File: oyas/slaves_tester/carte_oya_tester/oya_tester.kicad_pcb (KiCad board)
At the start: 2 copper layers, 99 x 99 mm, 54 parts, among them J1 Power, J2 Bus Oya, J3 Power_Bus, J4 ON_OFF, SW3 Address, SW4 Select, U1 D148K, U2 MAX485E, U3 BPC_Alim5V, X1 Trou, X2 Trou, X3 Trou, X4 Trou

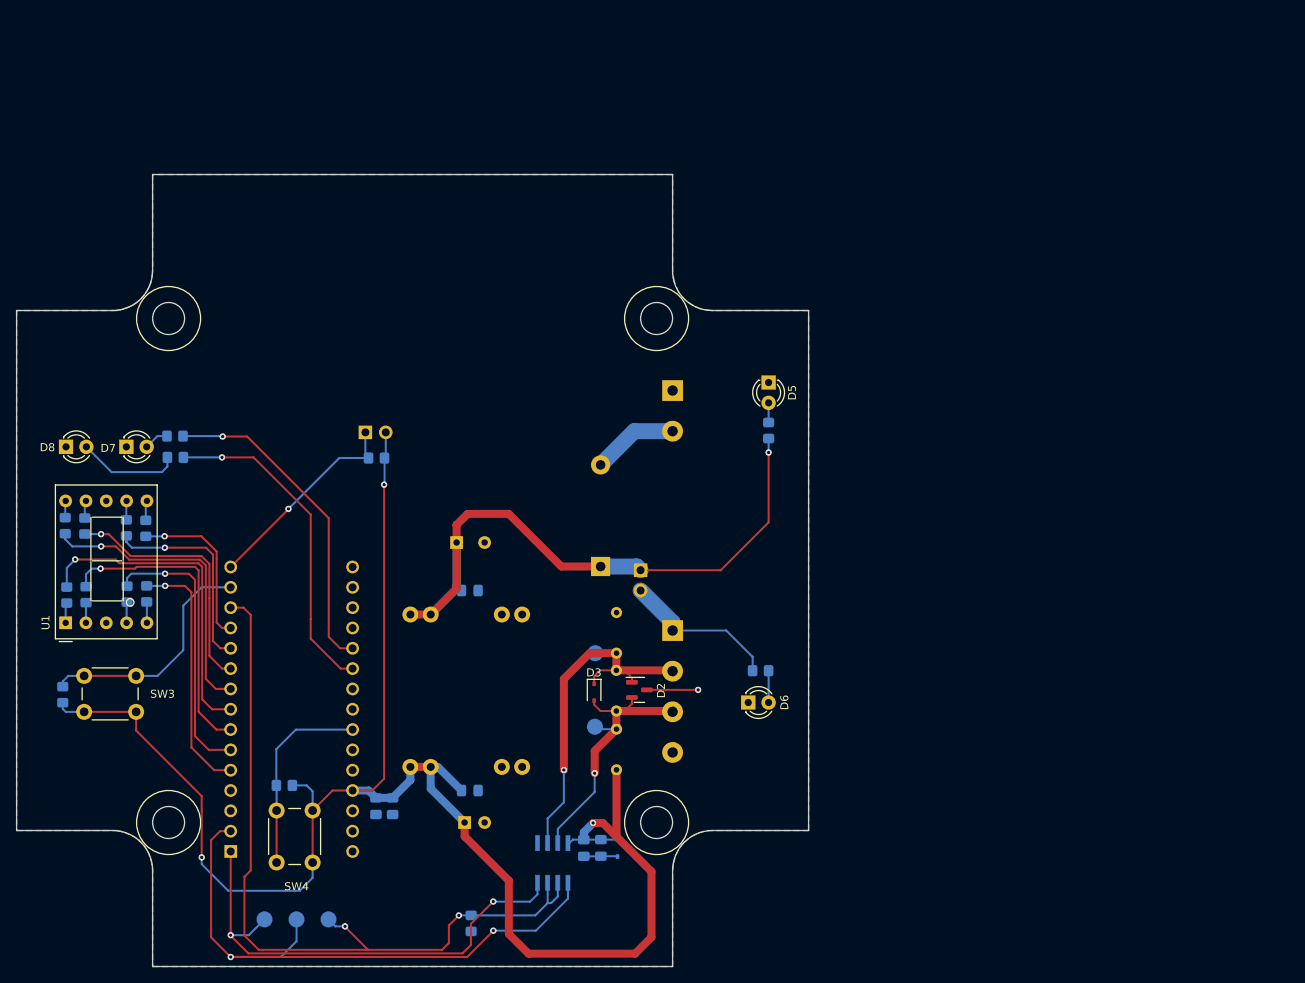
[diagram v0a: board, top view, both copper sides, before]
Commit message: Finalisation testeur Connecteurs des interrupteurs à choisir...
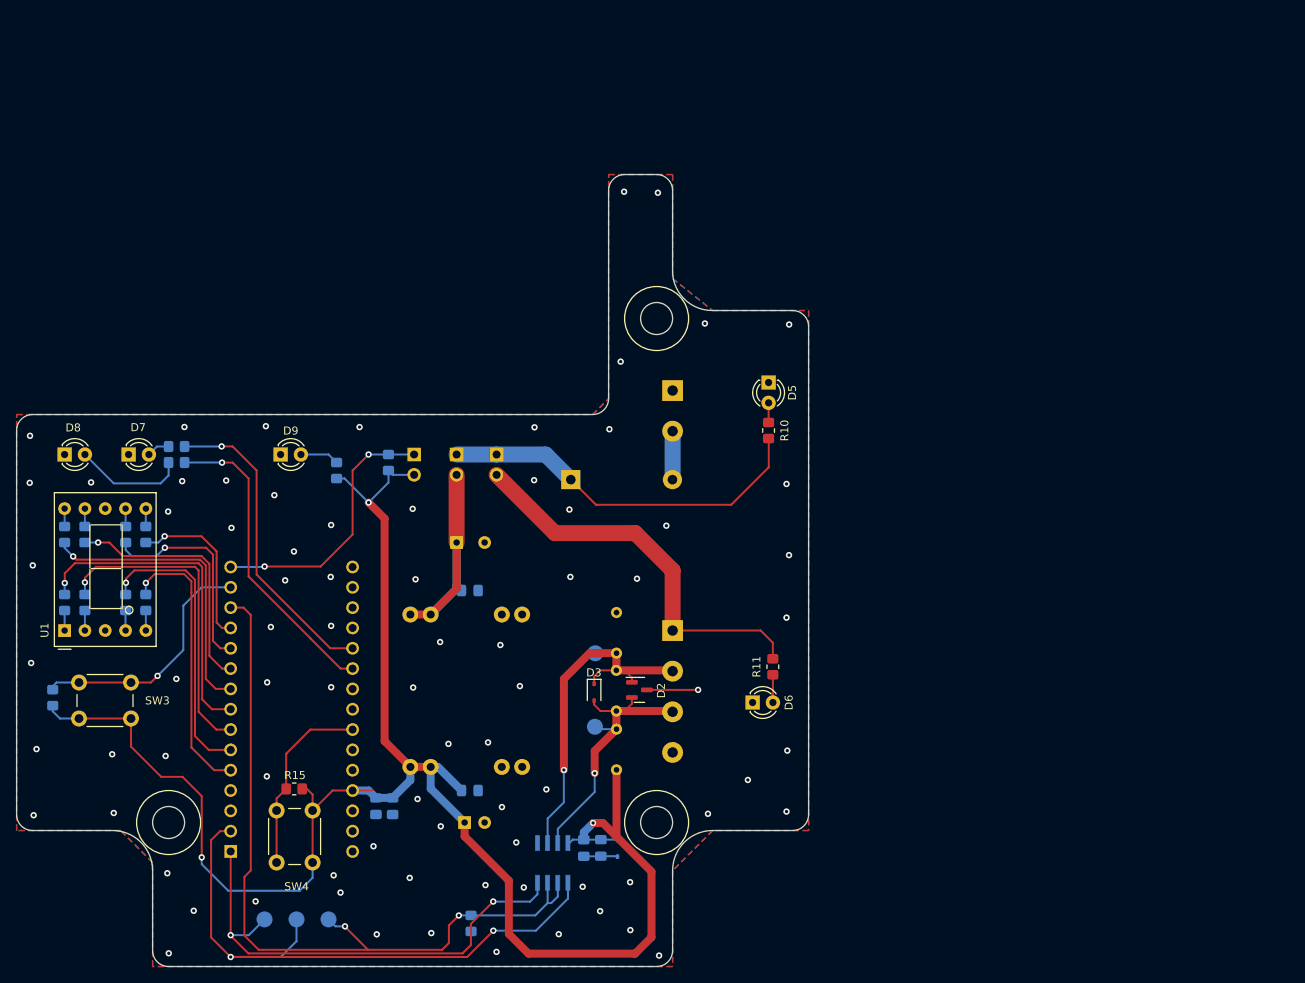
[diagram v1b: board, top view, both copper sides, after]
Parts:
- removed X1: Trou, bpc:BPC_Trou4mm_Fixation
- added D9: LED Rouge, LED_THT:LED_D3.0mm_FlatTop, F.Cu at (71.0, 98.0)
- added J5: Power_Cpu, Connector_PinHeader_2.54mm:PinHeader_1x02_P2.54mm_Vertical, B.Cu at (93.0, 98.0)
- added R20: 220, Resistor_SMD:R_0805_2012Metric_Pad1.20x1.40mm_HandSolder, B.Cu at (78.0, 100.0)
- R10, R11, R15: moved to F.Cu
- R12, R13: value 1k -> 220
- moved J3 23.1 mm to (98.0, 98.0)
- moved D4 11.5 mm to (107.3, 101.1), turned to 0 degrees
- moved J4 6.69 mm to (87.7, 98.0), turned to 180 degrees
- moved R11 1.61 mm to (132.5, 124.5), turned to -90 degrees
- moved R16 1.59 mm to (84.5, 99.0), turned to 90 degrees
- moved R12 1.32 mm to (58.0, 97.0)
- moved R14 1.31 mm to (42.5, 128.4)
- moved R15 1.31 mm to (72.7, 139.8)
- moved R7 1.10 mm to (44.0, 108.0)
- moved R8 1.09 mm to (54.1, 116.5)
- moved R3 1.07 mm to (51.6, 116.5)
- moved R6 1.06 mm to (46.5, 108.0)
- moved SW3 1.05 mm to (52.3, 131.0)
- moved D7 1.00 mm to (52.0, 98.0)
- moved R4 0.99 mm to (46.5, 116.5)
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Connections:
- C5 pad 1: POWER_12V -> Net-(J5-Pin_2)
- C8 pad 1: POWER_12V -> Net-(J5-Pin_2)
- U3 pad 1: POWER_12V -> Net-(J5-Pin_2)
- U3 pad 2: POWER_12V -> Net-(J5-Pin_2)
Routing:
- net POWER_12V: track 81.8 -> 47.2 mm, vias 1 -> 0
- net Net-(J5-Pin_2): track 0.00 -> 32.6 mm
- net Net-(J2-Pin_1): track 19.7 -> 49.6 mm
- net ON_OFF: track 26.3 -> 33.4 mm, vias 1 -> 2
- net Net-(D9-A): track 0.00 -> 4.87 mm
- net Net-(D4-A): track 10.7 -> 6.07 mm
- net +5V: track 213.8 -> 217.4 mm
- net SEG_DP: track 31.4 -> 34.8 mm
- net Net-(A1-A2): track 41.2 -> 38.8 mm
- net Net-(A1-A1): track 40.9 -> 39.1 mm
- net SEG_C: track 34.8 -> 36.3 mm
- net CHANGE_ADDRESS: track 29.8 -> 31.1 mm, vias 0 -> 1
- net Net-(D8-A): track 12.9 -> 14.0 mm
- net SELECT: track 24.7 -> 23.6 mm
- net SEG_D: track 38.8 -> 39.7 mm
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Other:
- outline, holes or cut-outs redrawn

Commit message: Finition
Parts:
- removed J3: Power_Bus, Connector_PinHeader_2.54mm:PinHeader_1x02_P2.54mm_Vertical
- removed J4: ON_OFF, Connector_PinHeader_2.54mm:PinHeader_1x02_P2.54mm_Vertical
- removed J5: Power_Cpu, Connector_PinHeader_2.54mm:PinHeader_1x02_P2.54mm_Vertical
- added C9: 1000µF, Capacitor_THT:CP_Radial_D16.0mm_P7.50mm, B.Cu at (116.6, 108.3)
- added J6: Switches, Connector_JST:JST_VH_B6P-VH-FB-B_1x06_P3.96mm_Vertical, B.Cu at (101.7, 99.3)
- C7, C8: moved to F.Cu
- moved R16 10.8 mm to (83.8, 109.8)
- moved D4 7.45 mm to (109.2, 108.3), turned to 90 degrees
- moved C5 5.18 mm to (92.9, 114.2)
- moved C8 5.08 mm to (94.7, 120.1)
- moved R20 3.88 mm to (74.5, 101.7), turned to 180 degrees
- moved U3 2.18 mm to (87.9, 120.1)
- moved C7 0.98 mm to (95.0, 139.1)
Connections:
- net +5V renamed SW_CMD_1
- net Net-(J2-Pin_1) renamed SW_BUS_2
- net Net-(J5-Pin_2) renamed SW_CPU_2
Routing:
- net GND: track 10.6 -> 24.1 mm, vias 80 -> 79
- net POWER_12V: track 47.2 -> 56.9 mm
- net SW_BUS_2: track 49.6 -> 58.5 mm
- net SW_CMD_1: track 217.4 -> 222.7 mm, vias 3 -> 4
- net Net-(D4-A): track 6.07 -> 11.0 mm
- net ON_OFF: track 33.4 -> 36.8 mm, vias 2 -> 1
- net SW_CPU_2: track 32.6 -> 29.9 mm
- net Net-(D9-A): track 4.87 -> 3.73 mm
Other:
- board text added: "Bus"
- board text added: "Cmd"
- board text added: "Cpu"
- board text added: "Switches"

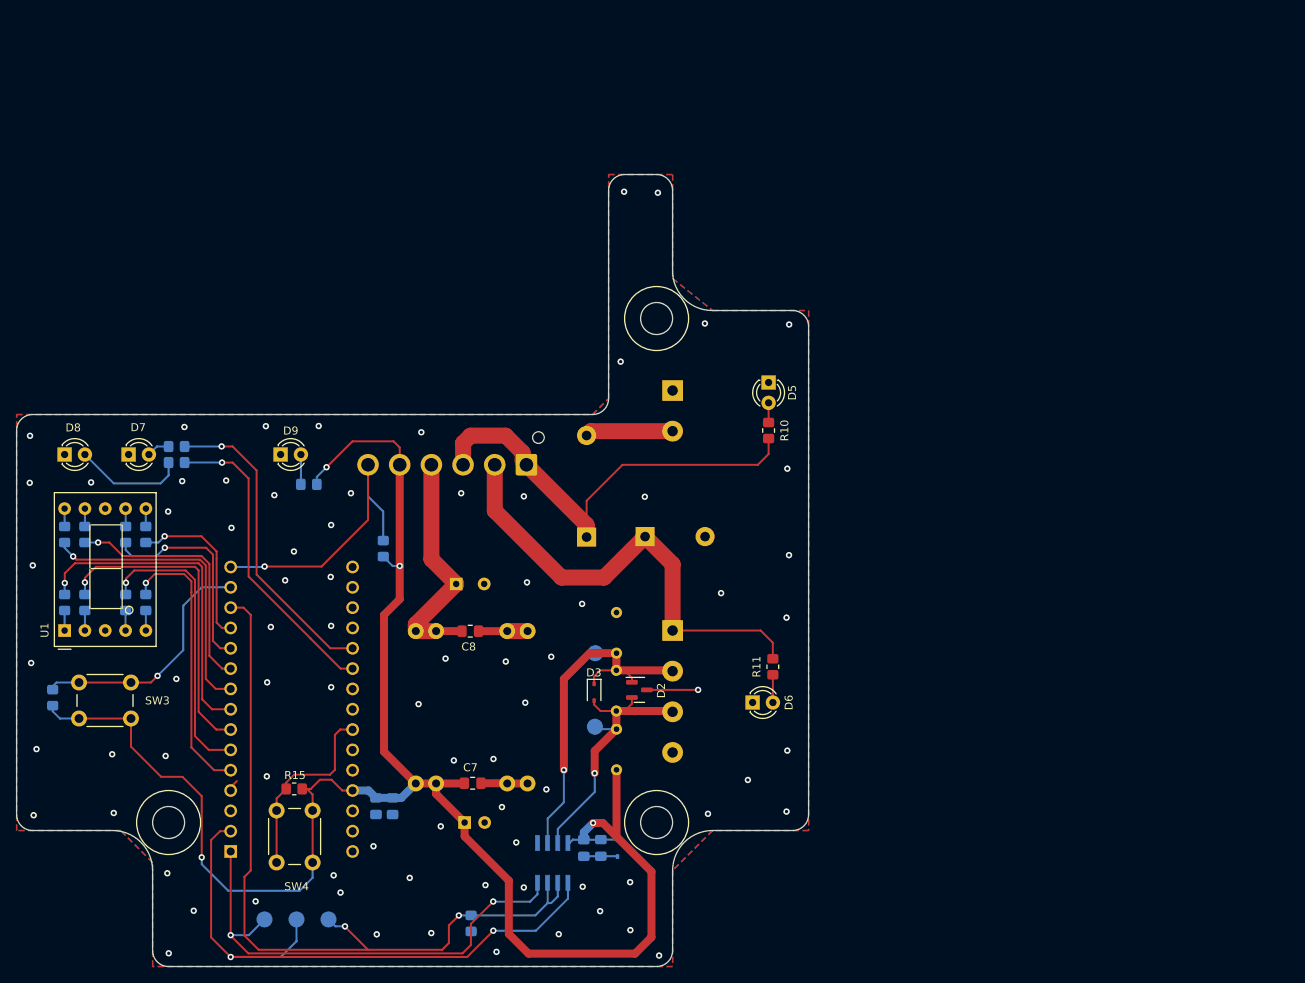
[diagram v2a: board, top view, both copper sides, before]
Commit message: Réception rev A et corrections: - Les SW étaient à 5V au lieu de GND - Idem sur le connecteur JST du SW ON/OFF - Valeur des résistances anodes du 7seg à 220 Ohms
Passage en Rev B pour la suivante

+ Ajout su soft de départ
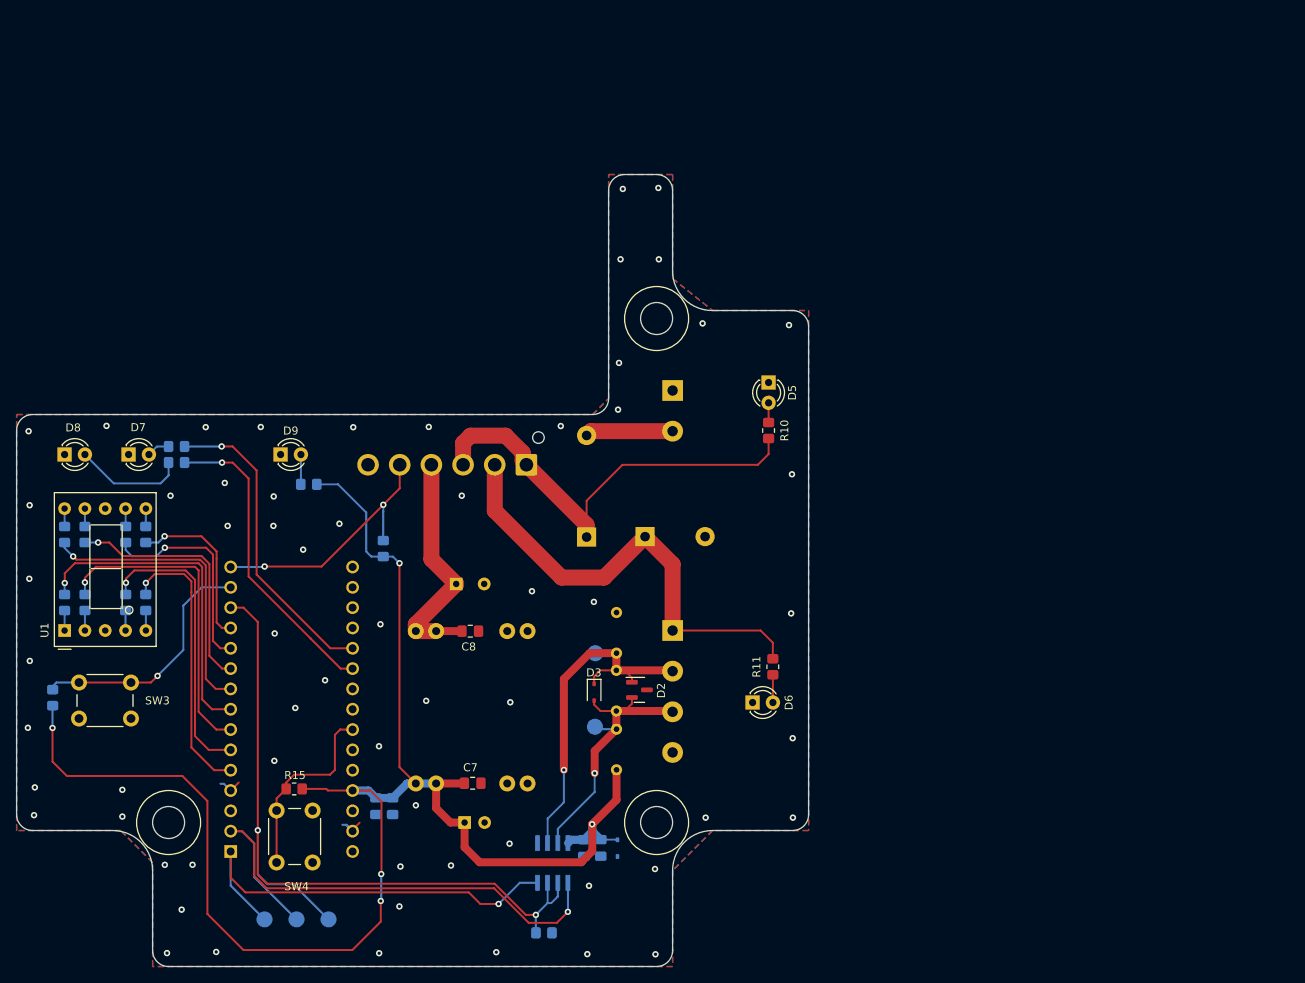
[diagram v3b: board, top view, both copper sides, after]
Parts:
- R1, R2, R3, R4, R5, R6, R7, R8: value R -> 220
- moved R9 9.19 mm to (103.9, 157.8), turned to 0 degrees
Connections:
- net SW_BUS_2 renamed SW_BUS
- net SW_CPU_2 renamed SW_CPU
- A1 pad 27: SW_CMD_1 -> +5V
- C1 pad 1: SW_CMD_1 -> +5V
- C2 pad 2: SW_CMD_1 -> +5V
- C3 pad 2: SW_CMD_1 -> +5V
- C4 pad 1: SW_CMD_1 -> +5V
- C6 pad 1: SW_CMD_1 -> +5V
- C7 pad 1: SW_CMD_1 -> +5V
- D1 pad 1: SW_CMD_1 -> +5V
- J6 pad 5: SW_CMD_1 -> ON_OFF
- J6 pad 6: ON_OFF -> GND
- R14 pad 1: SW_CMD_1 -> +5V
- R15 pad 1: SW_CMD_1 -> +5V
- R16 pad 1: SW_CMD_1 -> +5V
- R18 pad 1: SW_CMD_1 -> +5V
- R20 pad 1: SW_CMD_1 -> +5V
- SW3 pad 1: SW_CMD_1 -> GND
- SW4 pad 1: SW_CMD_1 -> GND
- U2 pad 8: SW_CMD_1 -> +5V
- U3 pad 7: SW_CMD_1 -> +5V
- U3 pad 8: SW_CMD_1 -> +5V
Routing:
- net SW_CMD_1: track 222.7 -> 0.00 mm, vias 4 -> 0
- net +5V: track 0.00 -> 202.1 mm, vias 0 -> 5
- net GND: track 24.1 -> 7.26 mm, vias 79 -> 62
- net RX: track 77.5 -> 68.8 mm, vias 2 -> 1
- net TX: track 60.9 -> 54.3 mm, vias 2 -> 1
- net ON_OFF: track 36.8 -> 32.6 mm, vias 1 -> 2
- net TX_EN: track 98.1 -> 99.6 mm
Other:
- board text added: "Testeur Oya Rev B 2026"
- board text removed: "Testeur Oya Rev A 2026"

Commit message: .
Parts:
- D1, D3: footprint Diode_SMD:D_SOD-323 -> bpc:BPC_D_SOD-323_HandSoldering
- D2: value SM712_SOT23 -> BPC_SM712_SOT23; footprint Package_TO_SOT_SMD:SOT-23 -> bpc:BPC_SOT-23-3_HandSoldering
- R18: value 4.7k -> R
